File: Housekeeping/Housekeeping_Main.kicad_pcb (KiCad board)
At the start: 2 copper layers, 80 x 80 mm, 103 parts, among them J1 Conn_ARM_JTAG_SWD_10, J2 Conn_02x26_Odd_Even, J3 Conn_02x26_Odd_Even, Q1 2N7002E, SW1 SW_Push, SW2 SW_Push, U1 STM32U575RITxQ, U10 TPS25947, U2 TPS25947, U3 TPS562200, U4 TPS562200, U6 INA219AxD, U7 INA219AxD, U8 TCAN1473ACDR-Q1, U9 LTC2986_HLX_-_1, Y1 32.768KHz, Y2 16MHz

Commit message: Added PC104 Cubesat Standard
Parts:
- removed J2, J3: Conn_02x26_Odd_Even, Connector_PinSocket_2.54mm:PinSocket_2x26_P2.54mm_Vertical
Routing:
- net +3V3: track 410.9 -> 280.7 mm, vias 13 -> 12
- net +5V: track 186.6 -> 146.2 mm
- net CANH: track 35.6 -> 20.2 mm
- net CANL: track 36.7 -> 21.6 mm
- net Net-(C25-Pad1): track 8.41 -> 0.00 mm

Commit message: PCB V2
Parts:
- removed H1, H2, H3, H4: MountingHole_Pad, MountingHole:MountingHole_2.5mm_Pad
- removed MT1, MT2: Screw_Terminal, TerminalBlock_Phoenix:TerminalBlock_Phoenix_MKDS-1,5-2-5.08_1x02_P5.08mm_Horizontal
- added U5: Payload, Payload PC104:PC104-Standard, F.Cu at (244.5, 50.2)
- moved R31 183.4 mm to (232.1, 55.1), turned to 0 degrees
- moved R30 179.3 mm to (232.1, 57.8), turned to 0 degrees
- moved C25 176.4 mm to (227.2, 55.1)
- moved U8 164.8 mm to (231.0, 66.4)
- moved C24 163.1 mm to (222.1, 66.2)
- moved C26 163.1 mm to (222.1, 63.0), turned to 0 degrees
- moved R28 163.0 mm to (221.9, 69.5)
- moved R29 158.5 mm to (232.0, 75.1), turned to 0 degrees
- moved C27 155.8 mm to (231.9, 78.1)
- moved J1 125.7 mm to (191.5, 47.3)
- moved C11 114.8 mm to (201.8, 97.8), turned to 0 degrees
- moved FB1 109.9 mm to (182.1, 104.0), turned to 0 degrees
- moved Q1 108.9 mm to (226.1, 123.7)
- moved R8 108.9 mm to (230.1, 120.9)
- moved R10 108.9 mm to (220.3, 116.9)
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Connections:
- net /MCU/SWCLK renamed SWCLK
- net /MCU/SWDIO renamed SWDIO
- U1 pad 42: unconnected-(U1-PA9-Pad42) -> TX1
- U1 pad 43: unconnected-(U1-PA10-Pad43) -> RX1
- U1 pad 8: unconnected-(U1-PC0-Pad8) -> RX2
- U1 pad 9: unconnected-(U1-PC1-Pad9) -> TX2
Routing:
- net +3V3: track 280.7 -> 388.5 mm, vias 12 -> 20
- net SDA: track 57.3 -> 132.2 mm, vias 8 -> 7
- net +5V: track 146.2 -> 212.9 mm
- net SCL: track 81.7 -> 145.6 mm, vias 5 -> 9
- net TX1: track 0.00 -> 58.8 mm, vias 0 -> 2
- net RX1: track 0.00 -> 58.0 mm, vias 0 -> 2
- net VBAT_Measured: track 64.0 -> 109.2 mm, vias 0 -> 2
- net CAN_nSTB: track 22.8 -> 64.2 mm
- net /MCU/Boot: track 57.4 -> 22.6 mm
- net V_BAT: track 24.4 -> 57.9 mm, vias 0 -> 2
- net /MCU/Reset: track 108.7 -> 79.0 mm, vias 4 -> 2
- net GND: track 42.3 -> 14.2 mm, vias 175 -> 363
- net CAN_EN: track 29.6 -> 54.7 mm
- net CAN_TX: track 35.2 -> 48.5 mm
- net TEMP_INTERRUPT: track 45.1 -> 32.6 mm
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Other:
- board size 80 x 80 mm -> 96 x 89.9 mm

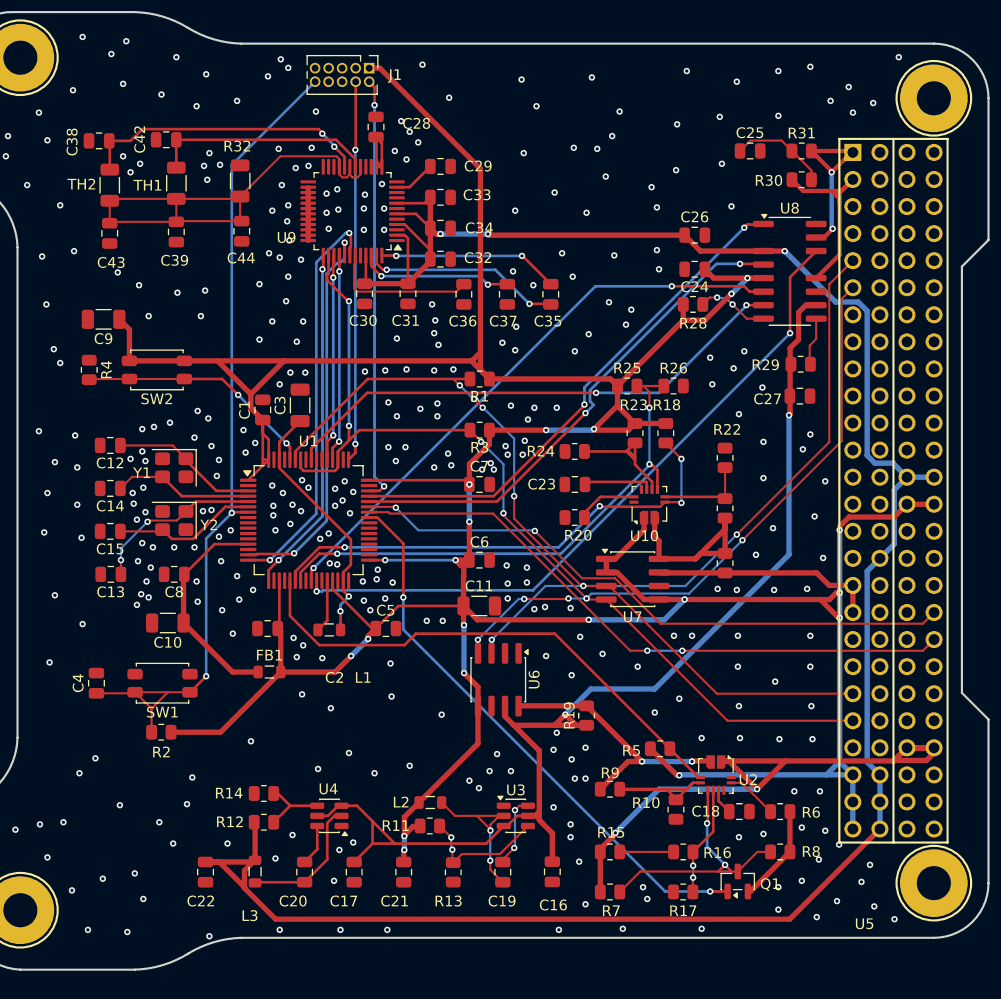
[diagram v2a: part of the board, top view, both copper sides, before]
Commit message: Added Radiation sensor and some minor changes
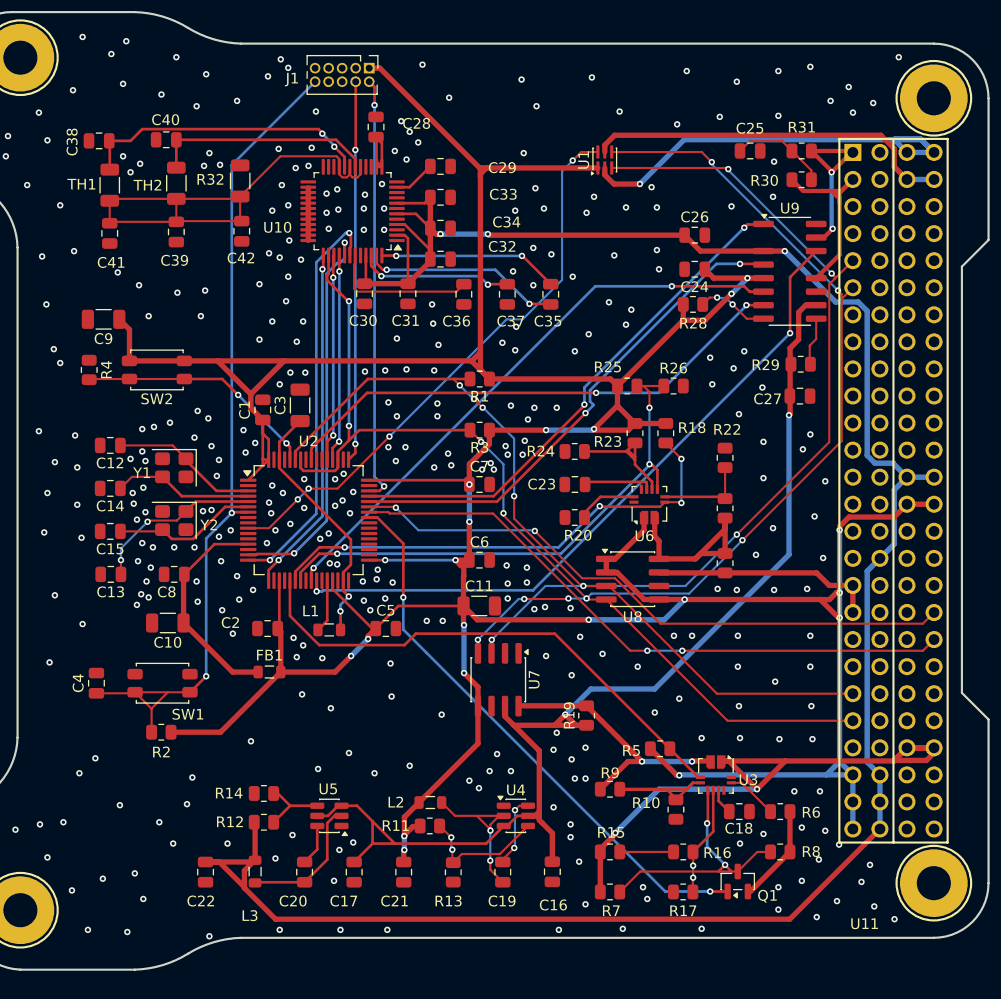
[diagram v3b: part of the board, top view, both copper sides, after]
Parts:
- added U1: FGD-04D, OptoDevice:Broadcom_DFN-6_2x2mm_P0.65mm, F.Cu at (213.6, 55.9)
- renumbered C42 to C40, C43 to C41, C44 to C42, TH2 to TH1, TH1 to TH2, U9 to U10, U5 to U11, U1 to U2, U2 to U3, U3 to U4, U4 to U5, U10 to U6, U6 to U7, U7 to U8, U8 to U9
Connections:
- U11 pad 53: unconnected-(U5-01-Pad53) -> VDOSE
- U11 pad 54: unconnected-(U5-02-Pad54) -> VDOSE
- U11 pad 55: unconnected-(U5-03-Pad55) -> GND
- U11 pad 56: unconnected-(U5-04-Pad56) -> GND
- U2 pad 10: unconnected-(U1-PC2-Pad10) -> VB
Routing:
- net VB: track 0.00 -> 53.5 mm, vias 0 -> 4
- net VDOSE: track 0.00 -> 46.3 mm, vias 0 -> 1
- net GND: track 14.2 -> 48.9 mm, vias 363 -> 357
- net SCL: track 145.6 -> 173.3 mm, vias 9 -> 11
- net SDA: track 132.2 -> 157.6 mm, vias 7 -> 9
- net +3V3: track 388.5 -> 400.6 mm

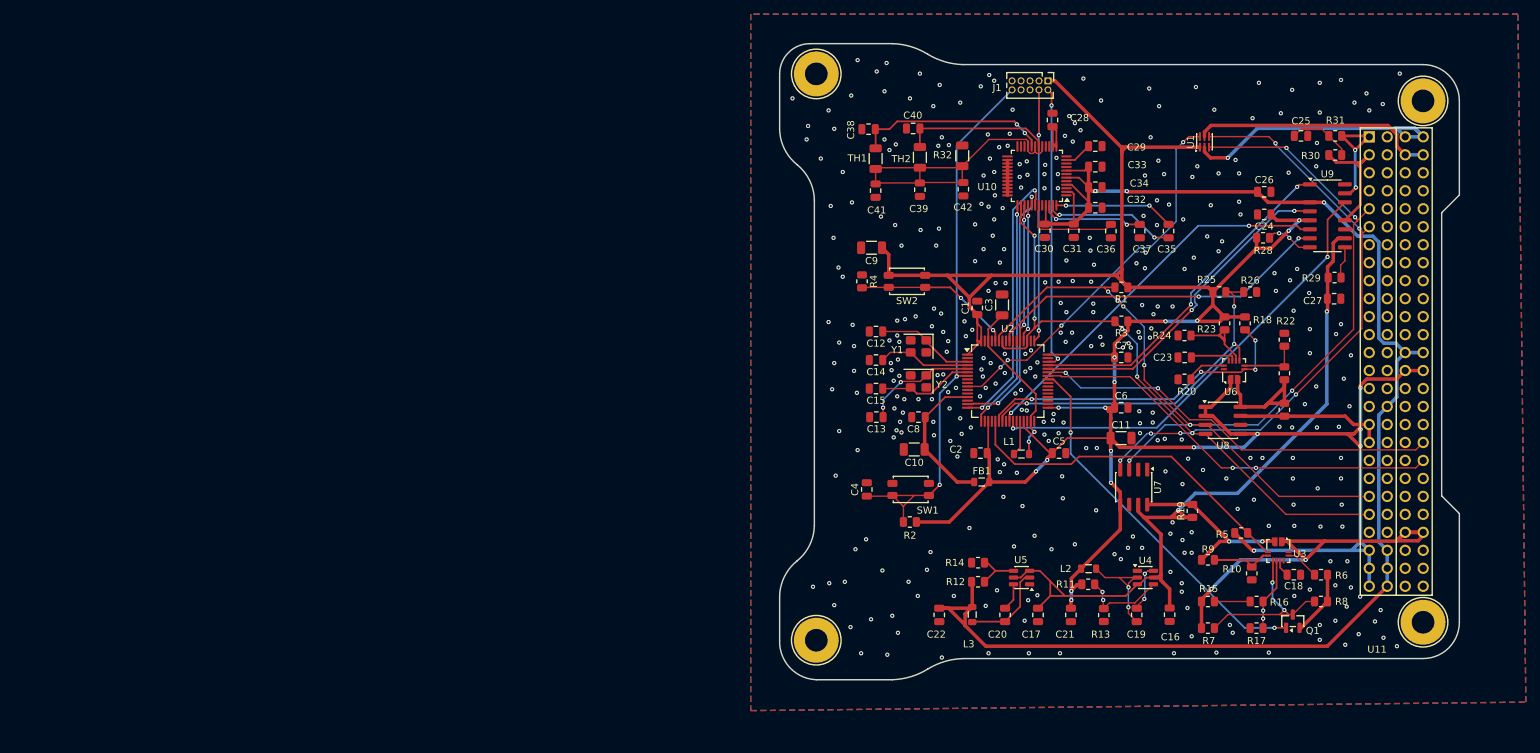
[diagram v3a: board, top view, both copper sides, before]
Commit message: Updated SWD Headers and other minor pcb changes
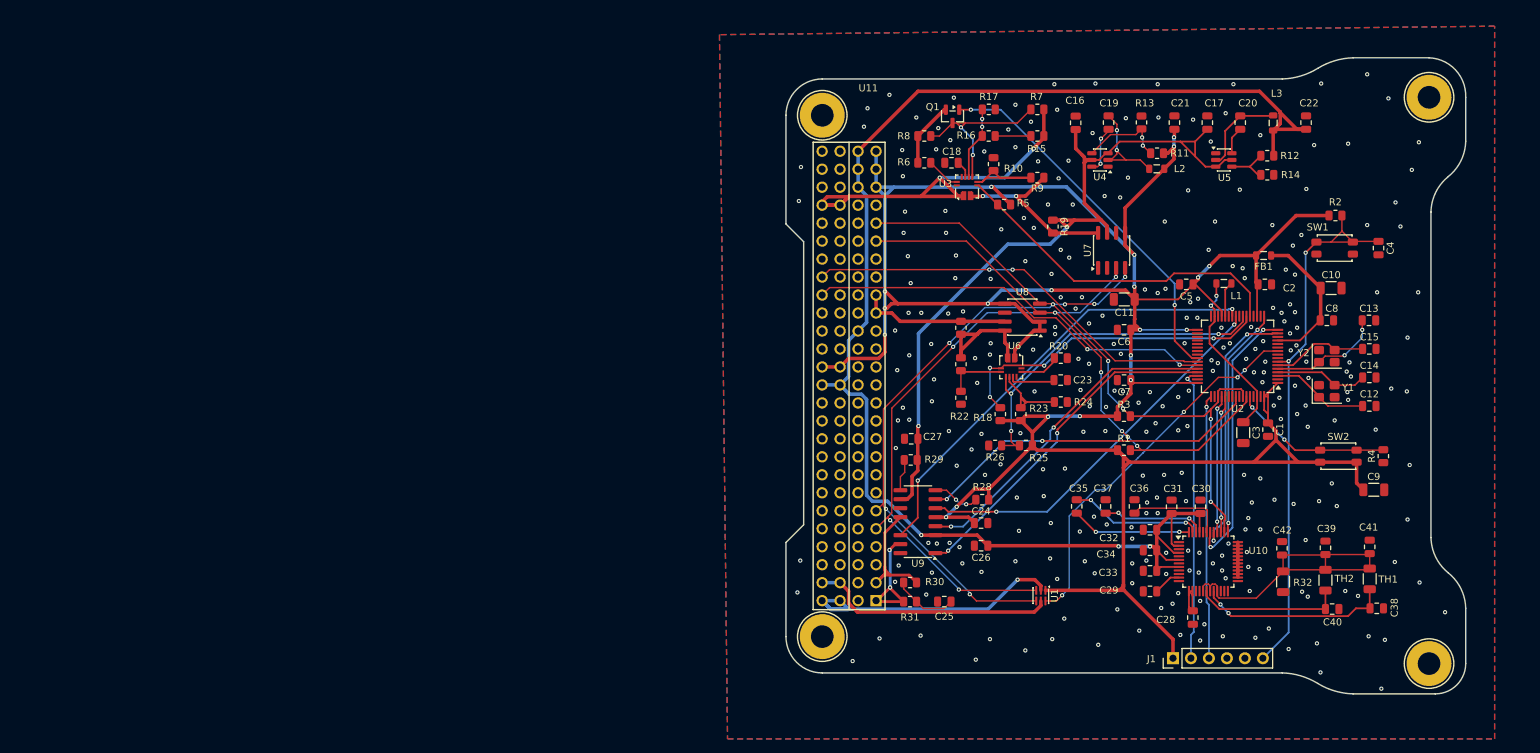
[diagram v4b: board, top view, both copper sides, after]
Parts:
- J1: value Conn_ARM_JTAG_SWD_10 -> Conn_01x06_Pin; footprint Connector_PinHeader_1.27mm:PinHeader_2x05_P1.27mm_Vertical -> Connector_PinHeader_2.54mm:PinHeader_1x06_P2.54mm_Vertical
- moved U11 113.7 mm to (159.6, 125.8), turned to 0 degrees
- moved C38 98.7 mm to (237.9, 121.8), turned to 180 degrees
- moved TH1 91.6 mm to (237.0, 117.7), turned to 90 degrees
- moved C40 90.1 mm to (231.7, 122.0), turned to 180 degrees
- moved R31 89.1 mm to (172.0, 120.9), turned to 180 degrees
- moved C22 86.7 mm to (228.0, 53.2), turned to -90 degrees
- moved R8 86.4 mm to (174.0, 55.1), turned to 180 degrees
- moved C41 86.1 mm to (237.0, 113.2), turned to 90 degrees
- moved Q1 86.0 mm to (178.0, 52.3), turned to -90 degrees
- moved R30 85.2 mm to (172.0, 118.2), turned to 180 degrees
- moved J1 83.5 mm to (209.2, 128.9), turned to 90 degrees
- moved C25 82.9 mm to (176.8, 120.9), turned to 180 degrees
- moved TH2 82.8 mm to (230.7, 117.9), turned to 90 degrees
- moved R17 82.5 mm to (183.1, 51.4), turned to 0 degrees
- moved L3 81.4 mm to (223.3, 53.3), turned to -90 degrees
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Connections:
- J1 pad 3: GND -> SWCLK
- J1 pad 4: SWCLK -> unconnected-(J1-Pin_4-Pad4)
- J1 pad 6: unconnected-(J1-SWO/TDO-Pad6) -> /MCU/Reset
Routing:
- net +3V3: track 400.6 -> 422.8 mm
- net SWCLK: track 35.8 -> 37.4 mm, vias 2 -> 1
- net SWDIO: track 40.1 -> 41.6 mm, vias 2 -> 1
- net CAN_RX: track 47.5 -> 46.9 mm
- net GND: vias 357 -> 285
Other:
- outline, holes or cut-outs redrawn

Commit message: Minor changes to PCB traces
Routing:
- net /Temeperature_Sensor/CH3: track 20.9 -> 24.6 mm
- net +3V3: track 422.8 -> 425.7 mm, vias 20 -> 21
- net VBAT_Protected: track 25.2 -> 26.5 mm
- net SCL: track 173.3 -> 174.4 mm
- net eFuse_Beacon_EN: track 51.5 -> 52.2 mm
